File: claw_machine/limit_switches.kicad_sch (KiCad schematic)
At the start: 5 parts, among them J24 Screw_Terminal_01x02, J25 Conn_01x02_Pin, SW24 SW_Push, SW25 SW_SPST

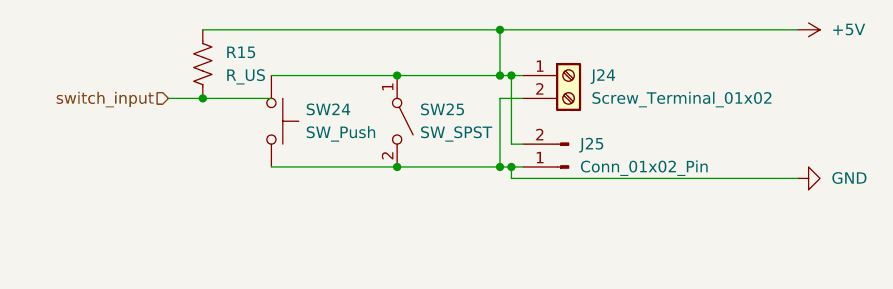
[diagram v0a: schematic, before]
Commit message: update limit switches to active high
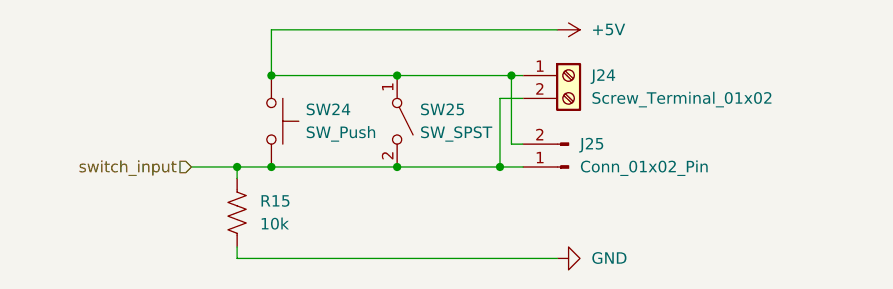
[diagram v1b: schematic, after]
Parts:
- R15: value R_US -> 10k
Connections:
- net +5V: no longer R15.2
- net GND: now also R15.1; no longer J24.2 (Pin_2), J25.1 (Pin_1), SW24.2, SW25.2 (B)
- net switch_input: now also J24.2 (Pin_2), J25.1 (Pin_1), R15.2, SW24.2, SW25.2 (B); no longer R15.1
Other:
- moved on the sheet: R15
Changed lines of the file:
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@@
   (junction (at 102.87 60.96) (diameter 0) (color 0 0 0 0)
   )
-  (junction (at 115.57 71.12) (diameter 0) (color 0 0 0 0)
+  (junction (at 88.9 71.12) (diameter 0) (color 0 0 0 0)
+  )
+  (junction (at 88.9 60.96) (diameter 0) (color 0 0 0 0)
   )
   (junction (at 102.87 71.12) (diameter 0) (color 0 0 0 0)
   )
-  (junction (at 114.3 60.96) (diameter 0) (color 0 0 0 0)
-  )
-  (junction (at 81.28 63.5) (diameter 0) (color 0 0 0 0)
-  )
   (junction (at 114.3 71.12) (diameter 0) (color 0 0 0 0)
   )
-  (junction (at 114.3 55.88) (diameter 0) (color 0 0 0 0)
+  (junction (at 85.09 71.12) (diameter 0) (color 0 0 0 0)
   )
   (junction (at 115.57 60.96) (diameter 0) (color 0 0 0 0)
   )
+  (wire (pts (xy 85.09 80.01) (xy 85.09 81.28))
+    (stroke (width 0) (type default))
+  )
   (wire (pts (xy 114.3 63.5) (xy 116.84 63.5))
     (stroke (width 0) (type default))
@@
     (stroke (width 0) (type default))
   )
-  (wire (pts (xy 81.28 63.5) (xy 88.9 63.5))
-    (stroke (width 0) (type default))
-  )
-  (wire (pts (xy 115.57 71.12) (xy 116.84 71.12))
-    (stroke (width 0) (type default))
-  )
-  (wire (pts (xy 115.57 71.12) (xy 115.57 72.39))
-    (stroke (width 0) (type default))
-  )
-  (wire (pts (xy 114.3 55.88) (xy 114.3 60.96))
-    (stroke (width 0) (type default))
-  )
-  (wire (pts (xy 115.57 72.39) (xy 147.32 72.39))
-    (stroke (width 0) (type default))
-  )
-  (wire (pts (xy 77.47 63.5) (xy 81.28 63.5))
+  (wire (pts (xy 85.09 71.12) (xy 88.9 71.12))
+    (stroke (width 0) (type default))
+  )
+  (wire (pts (xy 88.9 60.96) (xy 88.9 55.88))
+    (stroke (width 0) (type default))
+  )
+  (wire (pts (xy 114.3 71.12) (xy 116.84 71.12))
+    (stroke (width 0) (type default))
+  )
+  (wire (pts (xy 88.9 55.88) (xy 120.65 55.88))
+    (stroke (width 0) (type default))
+  )
+  (wire (pts (xy 85.09 71.12) (xy 85.09 72.39))
     (stroke (width 0) (type default))
   )
@@
     (stroke (width 0) (type default))
   )
-  (wire (pts (xy 114.3 55.88) (xy 147.32 55.88))
-    (stroke (width 0) (type default))
-  )
-  (wire (pts (xy 81.28 55.88) (xy 114.3 55.88))
+  (wire (pts (xy 85.09 81.28) (xy 120.65 81.28))
     (stroke (width 0) (type default))
   )
@@
     (stroke (width 0) (type default))
   )
-  (wire (pts (xy 102.87 60.96) (xy 114.3 60.96))
-    (stroke (width 0) (type default))
-  )
   (wire (pts (xy 115.57 60.96) (xy 115.57 68.58))
     (stroke (width 0) (type default))
@@
     (stroke (width 0) (type default))
   )
-  (wire (pts (xy 114.3 71.12) (xy 115.57 71.12))
-    (stroke (width 0) (type default))
-  )
   (wire (pts (xy 102.87 71.12) (xy 114.3 71.12))
     (stroke (width 0) (type default))
   )
-  (wire (pts (xy 114.3 60.96) (xy 115.57 60.96))
-    (stroke (width 0) (type default))
-  )
-  (hierarchical_label "switch_input" (shape input) (at 77.47 63.5 180) (fields_autoplaced)
+  (wire (pts (xy 80.01 71.12) (xy 85.09 71.12))
+    (stroke (width 0) (type default))
+  )
+  (wire (pts (xy 102.87 60.96) (xy 115.57 60.96))
+    (stroke (width 0) (type default))
+  )
+  (hierarchical_label "switch_input" (shape input) (at 80.01 71.12 180) (fields_autoplaced)
     (effects (font (size 1.27 1.27)) (justify right))
   )
-  (symbol (lib_id "Device:R_US") (at 81.28 59.69 180) (unit 1)
+  (symbol (lib_id "Device:R_US") (at 85.09 76.2 180) (unit 1)
     (in_bom yes) (on_board yes) (dnp no) (fields_autoplaced)
-    (property "Reference" "R15" (at 83.82 58.42 0)
+    (property "Reference" "R15" (at 87.63 74.93 0)
       (effects (font (size 1.27 1.27)) (justify right))
     )
-    (property "Value" "R_US" (at 83.82 60.96 0)
+    (property "Value" "10k" (at 87.63 77.47 0)
       (effects (font (size 1.27 1.27)) (justify right))
     )
-    (property "Footprint" "Resistor_SMD:R_0805_2012Metric_Pad1.20x1.40mm_HandSolder" (at 80.264 59.436 90)
-      (effects (font (size 1.27 1.27)) hide)
-    )
-    (property "Datasheet" "~" (at 81.28 59.69 0)
+    (property "Footprint" "Resistor_SMD:R_0805_2012Metric_Pad1.20x1.40mm_HandSolder" (at 84.074 75.946 90)
+      (effects (font (size 1.27 1.27)) hide)
+    )
+    (property "Datasheet" "~" (at 85.09 76.2 0)
       (effects (font (size 1.27 1.27)) hide)
     )
@@
     )
   )
-  (symbol (lib_id "power:+5V") (at 147.32 55.88 270) (unit 1)
+  (symbol (lib_id "power:+5V") (at 120.65 55.88 270) (unit 1)
     (in_bom yes) (on_board yes) (dnp no) (fields_autoplaced)
-    (property "Reference" "#PWR013" (at 143.51 55.88 0)
-      (effects (font (size 1.27 1.27)) hide)
-    )
-    (property "Value" "+5V" (at 151.13 55.88 90)
+    (property "Reference" "#PWR013" (at 116.84 55.88 0)
+      (effects (font (size 1.27 1.27)) hide)
+    )
+    (property "Value" "+5V" (at 124.46 55.88 90)
       (effects (font (size 1.27 1.27)) (justify left))
     )
-    (property "Footprint" "" (at 147.32 55.88 0)
-      (effects (font (size 1.27 1.27)) hide)
-    )
-    (property "Datasheet" "" (at 147.32 55.88 0)
+    (property "Footprint" "" (at 120.65 55.88 0)
+      (effects (font (size 1.27 1.27)) hide)
+    )
+    (property "Datasheet" "" (at 120.65 55.88 0)
       (effects (font (size 1.27 1.27)) hide)
     )
@@
     )
   )
-  (symbol (lib_id "power:GND") (at 147.32 72.39 90) (unit 1)
+  (symbol (lib_id "power:GND") (at 120.65 81.28 90) (unit 1)
     (in_bom yes) (on_board yes) (dnp no) (fields_autoplaced)
-    (property "Reference" "#PWR014" (at 153.67 72.39 0)
-      (effects (font (size 1.27 1.27)) hide)
-    )
-    (property "Value" "GND" (at 151.13 72.39 90)
+    (property "Reference" "#PWR014" (at 127 81.28 0)
+      (effects (font (size 1.27 1.27)) hide)
+    )
+    (property "Value" "GND" (at 124.46 81.28 90)
       (effects (font (size 1.27 1.27)) (justify right))
     )
-    (property "Footprint" "" (at 147.32 72.39 0)
-      (effects (font (size 1.27 1.27)) hide)
-    )
-    (property "Datasheet" "" (at 147.32 72.39 0)
-      (effects (font (size 1.27 1.27)) hide)
-    )
+    (property "Footprint" "" (at 120.65 81.28 0)
+      (effects (font (size 1.27 1.27)) hide)
+    )
+    (property "Datasheet" "" (at 120.65 81.28 0)
+      (effects (font (size 1.27 1.27)) hide)
+    )
